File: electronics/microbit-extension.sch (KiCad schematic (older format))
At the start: 25 parts, among them SW1 SW_DIP_x01, SW2 SW_DIP_x01, SW3 SW_DIP_x01, SW4 SW_DIP_x01

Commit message: moved footprints to separate folder
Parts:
- removed U?: TLC5917ID, SOIC127P600X175-16N, symbol TLC5917ID
- added BZ?: Buzzer, symbol Buzzer
- added C? (x2): C, symbol C
- added D?: D, symbol D
- added R? (x2): 1K, symbol R
- added T?: 2N4401, TO92-CBE, symbol 2N4401
- added U?: LD1117S33CTR, TO_SOT_Packages_SMD:SOT-223, symbol LD1117S33CTR
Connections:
- net labels added: +9V, AI1, BUZZER_PIN
- wire segments 53 -> 87

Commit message: footprint assignment
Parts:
- removed D?: D, symbol D
- removed R?: 1K, symbol R
- C1: renamed from C?; value C -> 100nF
- C2: renamed from C?; value C -> 10uF
- gave numbers to parts that had none: 24
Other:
- moved on the sheet: BZ1, R9, T1

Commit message: removed temp files
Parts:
- BZ1: footprint (none) -> Buzzers_Beepers:BUZZER
- C1, C2: footprint (none) -> Capacitors_SMD:C_1210
- D1, D2, D3, D4, D5: footprint (none) -> LEDs:LED_D3.0mm
- D6: footprint (none) -> LEDs:LED_RGB_5050-6
- J1: footprint (none) -> Connectors_4UCON:4UCON_17909_02x401.27mm_Vertical
- R1, R10, R11, R12, R13, R2, R3, R4, R5, R6, R7, R8, R9: footprint (none) -> Resistors_SMD:R_1210
- RV1: footprint (none) -> Potentiometers:Potentiometer_Alps_RK09K_Horizontal
- SW1, SW2, SW3, SW4: footprint (none) -> Buttons_Switches_SMD:SW_SPST_B3S-1100
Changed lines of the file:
@@
 F 0 "J1" H 1350 4700 50  0000 C CNN
 F 1 "microbit_edge_connector" H 1350 4600 50  0000 C CNN
-F 2 "" H 1200 2550 50  0001 C CNN
+F 2 "Connectors_4UCON:4UCON_17909_02x401.27mm_Vertical" H 1200 2550 50  0001 C CNN
 F 3 "" H 1200 2550 50  0001 C CNN
 	1    1300 2650
@@
 F 0 "SW1" H 10600 1600 50  0000 C CNN
 F 1 "SW_DIP_x01" H 10600 1300 50  0000 C CNN
-F 2 "" H 10600 1450 50  0001 C CNN
+F 2 "Buttons_Switches_SMD:SW_SPST_B3S-1100" H 10600 1450 50  0001 C CNN
 F 3 "" H 10600 1450 50  0001 C CNN
 	1    10600 1450
@@
 F 0 "R10" V 10230 1250 50  0000 C CNN
 F 1 "R" V 10150 1250 50  0000 C CNN
-F 2 "" V 10080 1250 50  0001 C CNN
+F 2 "Resistors_SMD:R_1210" V 10080 1250 50  0001 C CNN
 F 3 "" H 10150 1250 50  0001 C CNN
 	1    10150 1250
@@
 F 0 "SW2" H 10600 2150 50  0000 C CNN
 F 1 "SW_DIP_x01" H 10600 1850 50  0000 C CNN
-F 2 "" H 10600 2000 50  0001 C CNN
+F 2 "Buttons_Switches_SMD:SW_SPST_B3S-1100" H 10600 2000 50  0001 C CNN
 F 3 "" H 10600 2000 50  0001 C CNN
 	1    10600 2000
@@
 F 0 "R11" V 10230 1800 50  0000 C CNN
 F 1 "R" V 10150 1800 50  0000 C CNN
-F 2 "" V 10080 1800 50  0001 C CNN
+F 2 "Resistors_SMD:R_1210" V 10080 1800 50  0001 C CNN
 F 3 "" H 10150 1800 50  0001 C CNN
 	1    10150 1800
@@
 F 0 "SW3" H 10600 2700 50  0000 C CNN
 F 1 "SW_DIP_x01" H 10600 2400 50  0000 C CNN
-F 2 "" H 10600 2550 50  0001 C CNN
+F 2 "Buttons_Switches_SMD:SW_SPST_B3S-1100" H 10600 2550 50  0001 C CNN
 F 3 "" H 10600 2550 50  0001 C CNN
 	1    10600 2550
@@
 F 0 "R12" V 10230 2350 50  0000 C CNN
 F 1 "R" V 10150 2350 50  0000 C CNN
-F 2 "" V 10080 2350 50  0001 C CNN
+F 2 "Resistors_SMD:R_1210" V 10080 2350 50  0001 C CNN
 F 3 "" H 10150 2350 50  0001 C CNN
 	1    10150 2350
@@
 F 0 "SW4" H 10600 3150 50  0000 C CNN
 F 1 "SW_DIP_x01" H 10600 2850 50  0000 C CNN
-F 2 "" H 10600 3000 50  0001 C CNN
+F 2 "Buttons_Switches_SMD:SW_SPST_B3S-1100" H 10600 3000 50  0001 C CNN
 F 3 "" H 10600 3000 50  0001 C CNN
 	1    10600 3000
@@
 F 0 "R13" V 10230 2800 50  0000 C CNN
 F 1 "R" V 10150 2800 50  0000 C CNN
-F 2 "" V 10080 2800 50  0001 C CNN
+F 2 "Resistors_SMD:R_1210" V 10080 2800 50  0001 C CNN
 F 3 "" H 10150 2800 50  0001 C CNN
 	1    10150 2800
@@
 F 0 "RV1" V 10425 4150 50  0000 C CNN
 F 1 "POT" V 10500 4150 50  0000 C CNN
-F 2 "" H 10600 4150 50  0001 C CNN
+F 2 "Potentiometers:Potentiometer_Alps_RK09K_Horizontal" H 10600 4150 50  0001 C CNN
 F 3 "" H 10600 4150 50  0001 C CNN
 	1    10600 4150
@@
 F 0 "D1" H 8800 1250 50  0000 C CNN
 F 1 "LED" H 8800 1050 50  0000 C CNN
-F 2 "" H 8800 1150 50  0001 C CNN
+F 2 "LEDs:LED_D3.0mm" H 8800 1150 50  0001 C CNN
 F 3 "" H 8800 1150 50  0001 C CNN
 	1    8800 1150
@@
 F 0 "R1" V 8430 1150 50  0000 C CNN
 F 1 "R" V 8350 1150 50  0000 C CNN
-F 2 "" V 8280 1150 50  0001 C CNN
+F 2 "Resistors_SMD:R_1210" V 8280 1150 50  0001 C CNN
 F 3 "" H 8350 1150 50  0001 C CNN
 	1    8350 1150
@@
 F 0 "D3" H 8800 1850 50  0000 C CNN
 F 1 "LED" H 8800 1650 50  0000 C CNN
-F 2 "" H 8800 1750 50  0001 C CNN
+F 2 "LEDs:LED_D3.0mm" H 8800 1750 50  0001 C CNN
 F 3 "" H 8800 1750 50  0001 C CNN
 	1    8800 1750
@@
 F 0 "R3" V 8430 1750 50  0000 C CNN
 F 1 "R" V 8350 1750 50  0000 C CNN
-F 2 "" V 8280 1750 50  0001 C CNN
+F 2 "Resistors_SMD:R_1210" V 8280 1750 50  0001 C CNN
 F 3 "" H 8350 1750 50  0001 C CNN
 	1    8350 1750
@@
 F 0 "D2" H 8800 1550 50  0000 C CNN
 F 1 "LED" H 8800 1350 50  0000 C CNN
-F 2 "" H 8800 1450 50  0001 C CNN
+F 2 "LEDs:LED_D3.0mm" H 8800 1450 50  0001 C CNN
 F 3 "" H 8800 1450 50  0001 C CNN
 	1    8800 1450
@@
 F 0 "R2" V 8430 1450 50  0000 C CNN
 F 1 "R" V 8350 1450 50  0000 C CNN
-F 2 "" V 8280 1450 50  0001 C CNN
+F 2 "Resistors_SMD:R_1210" V 8280 1450 50  0001 C CNN
 F 3 "" H 8350 1450 50  0001 C CNN
 	1    8350 1450
@@
 F 0 "D4" H 8800 2150 50  0000 C CNN
 F 1 "LED" H 8800 1950 50  0000 C CNN
-F 2 "" H 8800 2050 50  0001 C CNN
+F 2 "LEDs:LED_D3.0mm" H 8800 2050 50  0001 C CNN
 F 3 "" H 8800 2050 50  0001 C CNN
 	1    8800 2050
@@
 F 0 "R4" V 8430 2050 50  0000 C CNN
 F 1 "R" V 8350 2050 50  0000 C CNN
-F 2 "" V 8280 2050 50  0001 C CNN
+F 2 "Resistors_SMD:R_1210" V 8280 2050 50  0001 C CNN
 F 3 "" H 8350 2050 50  0001 C CNN
 	1    8350 2050
@@
 F 0 "D5" H 8800 2450 50  0000 C CNN
 F 1 "LED" H 8800 2250 50  0000 C CNN
-F 2 "" H 8800 2350 50  0001 C CNN
+F 2 "LEDs:LED_D3.0mm" H 8800 2350 50  0001 C CNN
 F 3 "" H 8800 2350 50  0001 C CNN
 	1    8800 2350
@@
 F 0 "R5" V 8430 2350 50  0000 C CNN
 F 1 "R" V 8350 2350 50  0000 C CNN
-F 2 "" V 8280 2350 50  0001 C CNN
+F 2 "Resistors_SMD:R_1210" V 8280 2350 50  0001 C CNN
 F 3 "" H 8350 2350 50  0001 C CNN
 	1    8350 2350
@@
 F 0 "D6" H 8800 3320 50  0000 C CNN
 F 1 "LED_RGB" H 8800 2600 50  0000 C CNN
-F 2 "" H 8800 2900 50  0001 C CNN
+F 2 "LEDs:LED_RGB_5050-6" H 8800 2900 50  0001 C CNN
 F 3 "" H 8800 2900 50  0001 C CNN
 	1    8800 2950
@@
 F 0 "R6" V 8250 2750 50  0000 C CNN
 F 1 "R" V 8350 2750 50  0000 C CNN
-F 2 "" V 8280 2750 50  0001 C CNN
+F 2 "Resistors_SMD:R_1210" V 8280 2750 50  0001 C CNN
 F 3 "" H 8350 2750 50  0001 C CNN
 	1    8350 2750
@@
 F 0 "R7" V 8250 2950 50  0000 C CNN
 F 1 "R" V 8350 2950 50  0000 C CNN
-F 2 "" V 8280 2950 50  0001 C CNN
+F 2 "Resistors_SMD:R_1210" V 8280 2950 50  0001 C CNN
 F 3 "" H 8350 2950 50  0001 C CNN
 	1    8350 2950
@@
 F 0 "R8" V 8250 3150 50  0000 C CNN
 F 1 "R" V 8350 3150 50  0000 C CNN
-F 2 "" V 8280 3150 50  0001 C CNN
+F 2 "Resistors_SMD:R_1210" V 8280 3150 50  0001 C CNN
 F 3 "" H 8350 3150 50  0001 C CNN
 	1    8350 3150
@@
 F 0 "BZ1" H 10850 5300 50  0000 L CNN
 F 1 "Buzzer" H 10850 5200 50  0000 L CNN
-F 2 "" V 10675 5350 50  0001 C CNN
+F 2 "Buzzers_Beepers:BUZZER" V 10675 5350 50  0001 C CNN
 F 3 "" V 10675 5350 50  0001 C CNN
 	1    10700 5250
@@
 F 0 "R9" V 10280 5650 50  0000 C CNN
 F 1 "1K" V 10200 5650 50  0000 C CNN
-F 2 "" V 10130 5650 50  0001 C CNN
+F 2 "Resistors_SMD:R_1210" V 10130 5650 50  0001 C CNN
 F 3 "" H 10200 5650 50  0001 C CNN
 	1    10200 5650
@@
 F 0 "C1" H 8175 4500 50  0000 L CNN
 F 1 "100nF" H 8175 4300 50  0000 L CNN
-F 2 "" H 8188 4250 50  0001 C CNN
+F 2 "Capacitors_SMD:C_1210" H 8188 4250 50  0001 C CNN
 F 3 "" H 8150 4400 50  0001 C CNN
 	1    8150 4400
@@
 F 0 "C2" H 9225 4500 50  0000 L CNN
 F 1 "10uF" H 9225 4300 50  0000 L CNN
-F 2 "" H 9238 4250 50  0001 C CNN
+F 2 "Capacitors_SMD:C_1210" H 9238 4250 50  0001 C CNN
 F 3 "" H 9200 4400 50  0001 C CNN
 	1    9200 4400

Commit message: more updates to schematic
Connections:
- net +3V3: now also J1.17 (P18_3v3), J1.27 (P17_3v3)
- net AI1: now also J1.55 (P1), J1.57 (P1), J1.59 (P1), J1.61 (P1); no longer RV1.2
- net GND: now also J1.11 (P21_GND)
- net LED0: now also J1.29 (P16)
- net LED1: now also J1.45 (P12)
- net LED2: now also J1.49 (P10)
- net LED3: now also J1.51 (P9)
- net LED4: now also J1.53 (P8)
- net SDA: now reaches J1.13 (P20_SDA)
- net SCL: now reaches J1.15 (P19_SCL)
- net MOSI: now reaches J1.31 (P15_MOSI)
- net MISO: now reaches J1.33 (P14_MISO)
- net SCK: now reaches J1.35 (P13_SCK)
- net AI2: now reaches J1.37 (P2)
- net AI2: now also J1.39 (P2), J1.41 (P2), J1.43 (P2)
- net BUT_B: now reaches J1.47 (P11_Button_B)
- net BUT_A: now reaches J1.67 (P5_Button_A)
- net AI0: now reaches J1.71 (P0)
- net AI0: now also J1.73 (P0), J1.75 (P0), J1.77 (P0), RV1.2
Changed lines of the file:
@@
 $EndComp
 Wire Wire Line
-	1800 850  1800 1250
+	1800 850  1800 1350
 Connection ~ 1800 1150
 Connection ~ 1800 1050
@@
 Connection ~ 9050 2350
 Wire Wire Line
-	1800 1750 1800 2050
+	1800 1650 1800 2150
 Connection ~ 1800 1850
 Connection ~ 1800 1950
@@
 	10450 4150 9950 4150
 Text Label 9950 4150 0    60   ~ 0
-AI1
+AI0
 $Comp
 L Buzzer BZ1
@@
 Wire Wire Line
 	10600 5000 10600 5150
+Wire Wire Line
+	1800 2650 1800 2950
+Connection ~ 1800 2750
+Connection ~ 1800 2850
+Wire Wire Line
+	1800 3550 1800 3850
+Connection ~ 1800 3750
+Connection ~ 1800 3650
+Wire Wire Line
+	1800 3700 2100 3700
+Connection ~ 1800 3700
+Text Label 2100 3700 2    60   ~ 0
+AI1
+Wire Wire Line
+	1800 4350 1800 4650
+Connection ~ 1800 4450
+Connection ~ 1800 4550
+Text Label 2100 4500 2    60   ~ 0
+AI0
+Wire Wire Line
+	1800 4500 2100 4500
+Connection ~ 1800 4500
+Wire Wire Line
+	1800 2800 2100 2800
+Connection ~ 1800 2800
+Text Label 2100 2800 2    60   ~ 0
+AI2
+Connection ~ 1800 1750
+Connection ~ 1800 1250
+Wire Wire Line
+	1800 1450 2050 1450
+Wire Wire Line
+	1800 1550 2050 1550
+Text Label 2050 1450 2    60   ~ 0
+SDA
+Text Label 2050 1550 2    60   ~ 0
+SCL
+Wire Wire Line
+	1800 2350 2100 2350
+Wire Wire Line
+	1800 2450 2100 2450
+Wire Wire Line
+	1800 2550 2100 2550
+Text Label 2100 2350 2    60   ~ 0
+MOSI
+Text Label 2100 2450 2    60   ~ 0
+MISO
+Text Label 2100 2550 2    60   ~ 0
+SCK
+Connection ~ 1800 2050
+Wire Wire Line
+	1800 2250 2100 2250
+Text Label 2100 2250 2    60   ~ 0
+LED0
+Wire Wire Line
+	1800 3150 2100 3150
+Text Label 2100 3150 2    60   ~ 0
+BUT_B
+Wire Wire Line
+	1800 4150 2100 4150
+Text Label 2100 4150 2    60   ~ 0
+BUT_A
+Wire Wire Line
+	1800 3050 2100 3050
+Text Label 2100 3050 2    60   ~ 0
+LED1
+Wire Wire Line
+	1800 3250 2100 3250
+Text Label 2100 3250 2    60   ~ 0
+LED2
+Text Label 2100 3350 2    60   ~ 0
+LED3
+Wire Wire Line
+	1800 3350 2100 3350
+Wire Wire Line
+	1800 3450 2100 3450
+Text Label 2100 3450 2    60   ~ 0
+LED4
 $EndSCHEMATC

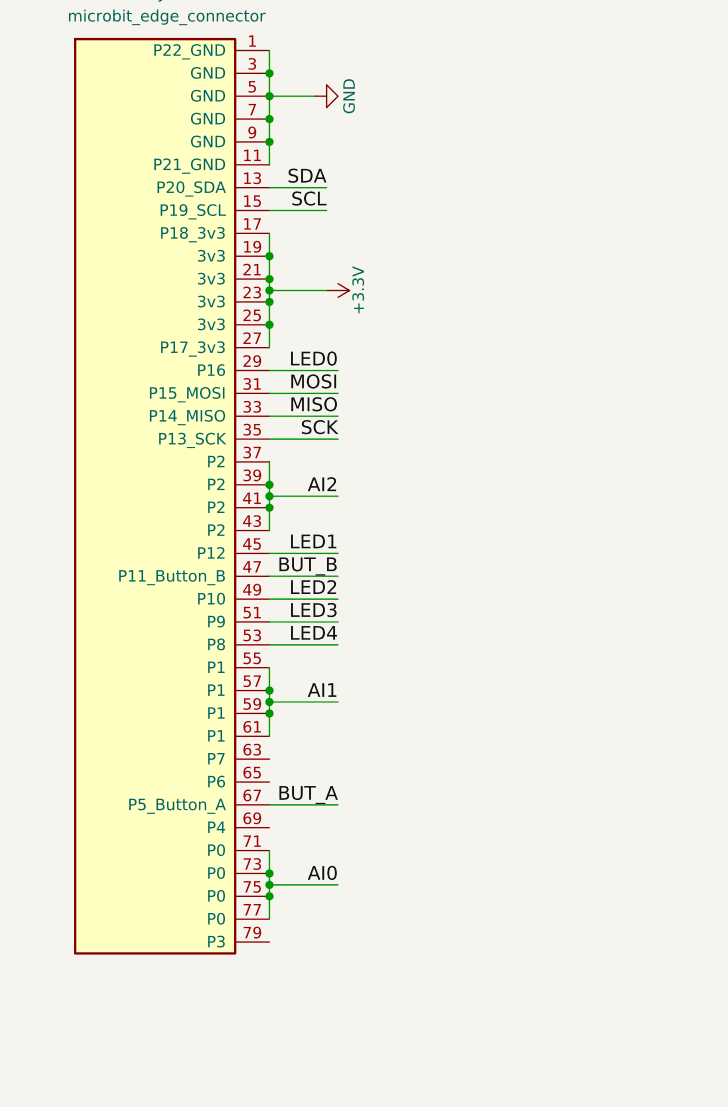
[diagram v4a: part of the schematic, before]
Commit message: added final local connections, need to check through
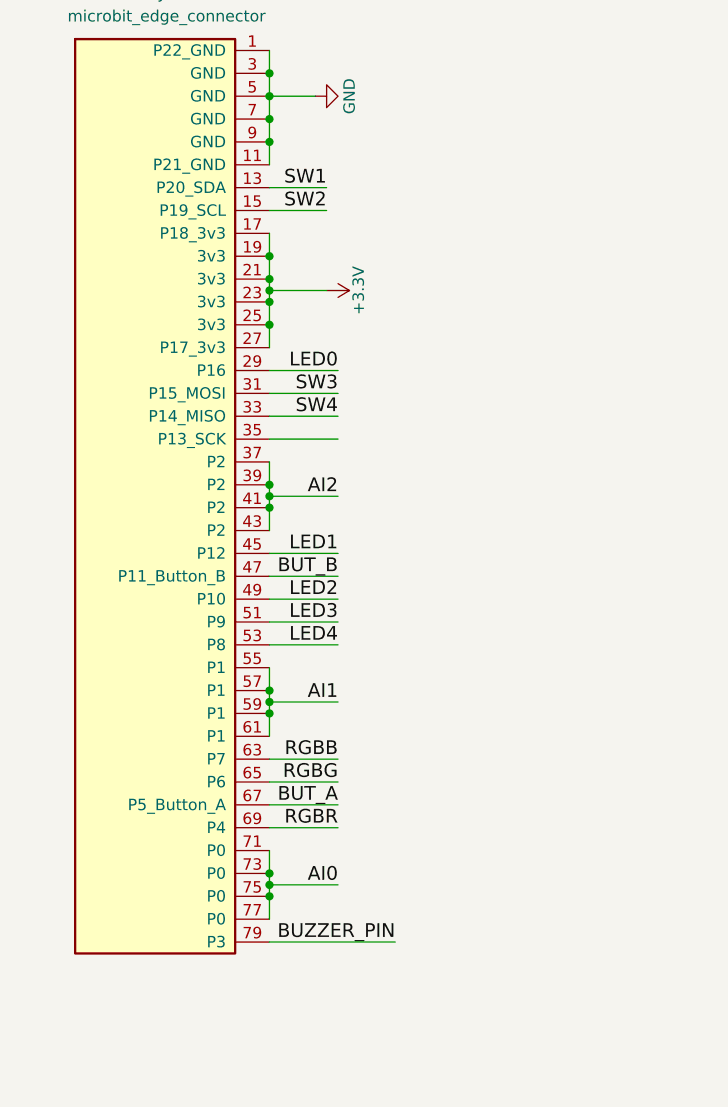
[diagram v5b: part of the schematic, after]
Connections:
- net MISO is gone; now on net SW4: J1.33 (P14_MISO)
- net MOSI is gone; now on net SW3: J1.31 (P15_MOSI)
- net SCL is gone; now on net SW2: J1.15 (P19_SCL)
- net SDA is gone; now on net SW1: J1.13 (P20_SDA)
- net BUZZER_PIN: now also J1.79 (P3)
- net RGBB: now also J1.63 (P7)
- net RGBG: now also J1.65 (P6)
- net RGBR: now also J1.69 (P4)
- net SCK: no longer names the net of J1.35 (P13_SCK)
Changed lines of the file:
@@
 Wire Wire Line
 	1800 1550 2050 1550
-Text Label 2050 1450 2    60   ~ 0
-SDA
-Text Label 2050 1550 2    60   ~ 0
-SCL
 Wire Wire Line
 	1800 2350 2100 2350
@@
 Wire Wire Line
 	1800 2550 2100 2550
-Text Label 2100 2350 2    60   ~ 0
-MOSI
-Text Label 2100 2450 2    60   ~ 0
-MISO
-Text Label 2100 2550 2    60   ~ 0
-SCK
 Connection ~ 1800 2050
 Wire Wire Line
@@
 Text Label 2100 3450 2    60   ~ 0
 LED4
+Text Label 2100 3950 2    60   ~ 0
+RGBB
+Wire Wire Line
+	1800 3950 2100 3950
+Wire Wire Line
+	1800 4050 2100 4050
+Text Label 2100 4050 2    60   ~ 0
+RGBG
+Wire Wire Line
+	1800 4250 2100 4250
+Text Label 2100 4250 2    60   ~ 0
+RGBR
+Wire Wire Line
+	1800 4750 2350 4750
+Text Label 2050 1450 2    60   ~ 0
+SW1
+Text Label 2050 1550 2    60   ~ 0
+SW2
+Text Label 2100 2350 2    60   ~ 0
+SW3
+Text Label 2100 2450 2    60   ~ 0
+SW4
+Text Label 2350 4750 2    60   ~ 0
+BUZZER_PIN
 $EndSCHEMATC

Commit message: update to schematics
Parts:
- C1, C2: footprint Capacitors_SMD:C_1210 -> Capacitors_SMD:C_0805
- R1, R10, R11, R12, R13, R2, R3, R4, R5, R6, R7, R8, R9: footprint Resistors_SMD:R_1210 -> Resistors_SMD:R_0805
- SW1, SW2, SW3, SW4: footprint Buttons_Switches_SMD:SW_SPST_B3S-1100 -> Buttons_Switches_SMD:SW_SPST_EVPBF
- T1: footprint TO92-CBE -> (none)
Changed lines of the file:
@@
 F 0 "SW1" H 10600 1600 50  0000 C CNN
 F 1 "SW_DIP_x01" H 10600 1300 50  0000 C CNN
-F 2 "Buttons_Switches_SMD:SW_SPST_B3S-1100" H 10600 1450 50  0001 C CNN
+F 2 "Buttons_Switches_SMD:SW_SPST_EVPBF" H 10600 1450 50  0001 C CNN
 F 3 "" H 10600 1450 50  0001 C CNN
 	1    10600 1450
@@
 F 0 "R10" V 10230 1250 50  0000 C CNN
 F 1 "R" V 10150 1250 50  0000 C CNN
-F 2 "Resistors_SMD:R_1210" V 10080 1250 50  0001 C CNN
+F 2 "Resistors_SMD:R_0805" V 10080 1250 50  0001 C CNN
 F 3 "" H 10150 1250 50  0001 C CNN
 	1    10150 1250
@@
 F 0 "SW2" H 10600 2150 50  0000 C CNN
 F 1 "SW_DIP_x01" H 10600 1850 50  0000 C CNN
-F 2 "Buttons_Switches_SMD:SW_SPST_B3S-1100" H 10600 2000 50  0001 C CNN
+F 2 "Buttons_Switches_SMD:SW_SPST_EVPBF" H 10600 2000 50  0001 C CNN
 F 3 "" H 10600 2000 50  0001 C CNN
 	1    10600 2000
@@
 F 0 "R11" V 10230 1800 50  0000 C CNN
 F 1 "R" V 10150 1800 50  0000 C CNN
-F 2 "Resistors_SMD:R_1210" V 10080 1800 50  0001 C CNN
+F 2 "Resistors_SMD:R_0805" V 10080 1800 50  0001 C CNN
 F 3 "" H 10150 1800 50  0001 C CNN
 	1    10150 1800
@@
 F 0 "SW3" H 10600 2700 50  0000 C CNN
 F 1 "SW_DIP_x01" H 10600 2400 50  0000 C CNN
-F 2 "Buttons_Switches_SMD:SW_SPST_B3S-1100" H 10600 2550 50  0001 C CNN
+F 2 "Buttons_Switches_SMD:SW_SPST_EVPBF" H 10600 2550 50  0001 C CNN
 F 3 "" H 10600 2550 50  0001 C CNN
 	1    10600 2550
@@
 F 0 "R12" V 10230 2350 50  0000 C CNN
 F 1 "R" V 10150 2350 50  0000 C CNN
-F 2 "Resistors_SMD:R_1210" V 10080 2350 50  0001 C CNN
+F 2 "Resistors_SMD:R_0805" V 10080 2350 50  0001 C CNN
 F 3 "" H 10150 2350 50  0001 C CNN
 	1    10150 2350
@@
 F 0 "SW4" H 10600 3150 50  0000 C CNN
 F 1 "SW_DIP_x01" H 10600 2850 50  0000 C CNN
-F 2 "Buttons_Switches_SMD:SW_SPST_B3S-1100" H 10600 3000 50  0001 C CNN
+F 2 "Buttons_Switches_SMD:SW_SPST_EVPBF" H 10600 3000 50  0001 C CNN
 F 3 "" H 10600 3000 50  0001 C CNN
 	1    10600 3000
@@
 F 0 "R13" V 10230 2800 50  0000 C CNN
 F 1 "R" V 10150 2800 50  0000 C CNN
-F 2 "Resistors_SMD:R_1210" V 10080 2800 50  0001 C CNN
+F 2 "Resistors_SMD:R_0805" V 10080 2800 50  0001 C CNN
 F 3 "" H 10150 2800 50  0001 C CNN
 	1    10150 2800
@@
 F 0 "R1" V 8430 1150 50  0000 C CNN
 F 1 "R" V 8350 1150 50  0000 C CNN
-F 2 "Resistors_SMD:R_1210" V 8280 1150 50  0001 C CNN
+F 2 "Resistors_SMD:R_0805" V 8280 1150 50  0001 C CNN
 F 3 "" H 8350 1150 50  0001 C CNN
 	1    8350 1150
@@
 F 0 "R3" V 8430 1750 50  0000 C CNN
 F 1 "R" V 8350 1750 50  0000 C CNN
-F 2 "Resistors_SMD:R_1210" V 8280 1750 50  0001 C CNN
+F 2 "Resistors_SMD:R_0805" V 8280 1750 50  0001 C CNN
 F 3 "" H 8350 1750 50  0001 C CNN
 	1    8350 1750
@@
 F 0 "R2" V 8430 1450 50  0000 C CNN
 F 1 "R" V 8350 1450 50  0000 C CNN
-F 2 "Resistors_SMD:R_1210" V 8280 1450 50  0001 C CNN
+F 2 "Resistors_SMD:R_0805" V 8280 1450 50  0001 C CNN
 F 3 "" H 8350 1450 50  0001 C CNN
 	1    8350 1450
@@
 F 0 "R4" V 8430 2050 50  0000 C CNN
 F 1 "R" V 8350 2050 50  0000 C CNN
-F 2 "Resistors_SMD:R_1210" V 8280 2050 50  0001 C CNN
+F 2 "Resistors_SMD:R_0805" V 8280 2050 50  0001 C CNN
 F 3 "" H 8350 2050 50  0001 C CNN
 	1    8350 2050
@@
 F 0 "R5" V 8430 2350 50  0000 C CNN
 F 1 "R" V 8350 2350 50  0000 C CNN
-F 2 "Resistors_SMD:R_1210" V 8280 2350 50  0001 C CNN
+F 2 "Resistors_SMD:R_0805" V 8280 2350 50  0001 C CNN
 F 3 "" H 8350 2350 50  0001 C CNN
 	1    8350 2350
@@
 F 0 "R6" V 8250 2750 50  0000 C CNN
 F 1 "R" V 8350 2750 50  0000 C CNN
-F 2 "Resistors_SMD:R_1210" V 8280 2750 50  0001 C CNN
+F 2 "Resistors_SMD:R_0805" V 8280 2750 50  0001 C CNN
 F 3 "" H 8350 2750 50  0001 C CNN
 	1    8350 2750
@@
 F 0 "R7" V 8250 2950 50  0000 C CNN
 F 1 "R" V 8350 2950 50  0000 C CNN
-F 2 "Resistors_SMD:R_1210" V 8280 2950 50  0001 C CNN
+F 2 "Resistors_SMD:R_0805" V 8280 2950 50  0001 C CNN
 F 3 "" H 8350 2950 50  0001 C CNN
 	1    8350 2950
@@
 F 0 "R8" V 8250 3150 50  0000 C CNN
 F 1 "R" V 8350 3150 50  0000 C CNN
-F 2 "Resistors_SMD:R_1210" V 8280 3150 50  0001 C CNN
+F 2 "Resistors_SMD:R_0805" V 8280 3150 50  0001 C CNN
 F 3 "" H 8350 3150 50  0001 C CNN
 	1    8350 3150
@@
 F 0 "T1" H 10099 5950 50  0000 L BNN
 F 1 "2N4401" H 10100 5850 50  0000 L BNN
-F 2 "TO92-CBE" H 10500 5650 50  0001 L BNN
+F 2 "" H 10500 5650 50  0001 L BNN
 F 3 "Multicomp" H 10500 5650 50  0001 L BNN
 F 4 "BIPOLAR TRANSISTOR%2C NPN%2C TO-92%3B Transistor Polarity%3A NPN%3B Collector Emitter Voltage V%28br%29ceo%3A 40V%3B Transition Frequen..." H 10500 5650 50  0001 L BNN "Description"
@@
 F 0 "R9" V 10280 5650 50  0000 C CNN
 F 1 "1K" V 10200 5650 50  0000 C CNN
-F 2 "Resistors_SMD:R_1210" V 10130 5650 50  0001 C CNN
+F 2 "Resistors_SMD:R_0805" V 10130 5650 50  0001 C CNN
 F 3 "" H 10200 5650 50  0001 C CNN
 	1    10200 5650
@@
 F 0 "C1" H 8175 4500 50  0000 L CNN
 F 1 "100nF" H 8175 4300 50  0000 L CNN
-F 2 "Capacitors_SMD:C_1210" H 8188 4250 50  0001 C CNN
+F 2 "Capacitors_SMD:C_0805" H 8188 4250 50  0001 C CNN
 F 3 "" H 8150 4400 50  0001 C CNN
 	1    8150 4400
@@
 F 0 "C2" H 9225 4500 50  0000 L CNN
 F 1 "10uF" H 9225 4300 50  0000 L CNN
-F 2 "Capacitors_SMD:C_1210" H 9238 4250 50  0001 C CNN
+F 2 "Capacitors_SMD:C_0805" H 9238 4250 50  0001 C CNN
 F 3 "" H 9200 4400 50  0001 C CNN
 	1    9200 4400

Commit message: finishing up routing
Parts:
- added J2: 9V conn, Pin_Headers:Pin_Header_Straight_1x02_Pitch2.54mm, symbol CONN_01X02
- T1: footprint (none) -> TO_SOT_Packages_SMD:SOT-23
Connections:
- net +9V: now also J2.1 (P1)
- net GND: now also J2.2 (P2)
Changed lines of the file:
@@
 F 0 "T1" H 10099 5950 50  0000 L BNN
 F 1 "2N4401" H 10100 5850 50  0000 L BNN
-F 2 "" H 10500 5650 50  0001 L BNN
+F 2 "TO_SOT_Packages_SMD:SOT-23" H 10500 5650 50  0001 L BNN
 F 3 "Multicomp" H 10500 5650 50  0001 L BNN
 F 4 "BIPOLAR TRANSISTOR%2C NPN%2C TO-92%3B Transistor Polarity%3A NPN%3B Collector Emitter Voltage V%28br%29ceo%3A 40V%3B Transition Frequen..." H 10500 5650 50  0001 L BNN "Description"
@@
 	0    1    1    0
 $EndComp
-Wire Wire Line
-	10350 5650 10400 5650
 $Comp
 L GND #PWR012
@@
 	0    1    1    0
 $EndComp
-Wire Wire Line
-	10600 5350 10600 5450
 Wire Wire Line
 	10600 5000 10600 5150
@@
 Text Label 2350 4750 2    60   ~ 0
 BUZZER_PIN
+$Comp
+L CONN_01X02 J2
+U 1 1 598C7F0A
+P 8650 5300
+F 0 "J2" H 8650 5450 50  0000 C CNN
+F 1 "9V conn" V 8750 5300 50  0000 C CNN
+F 2 "Pin_Headers:Pin_Header_Straight_1x02_Pitch2.54mm" H 8650 5300 50  0001 C CNN
+F 3 "" H 8650 5300 50  0001 C CNN
+	1    8650 5300
+	1    0    0    -1
+$EndComp
+$Comp
+L +9V #PWR016
+U 1 1 598C8024
+P 8450 5250
+F 0 "#PWR016" H 8450 5100 50  0001 C CNN
+F 1 "+9V" H 8450 5390 50  0000 C CNN
+F 2 "" H 8450 5250 50  0001 C CNN
+F 3 "" H 8450 5250 50  0001 C CNN
+	1    8450 5250
+	0    -1   -1   0
+$EndComp
+$Comp
+L GND #PWR017
+U 1 1 598C808C
+P 8450 5350
+F 0 "#PWR017" H 8450 5100 50  0001 C CNN
+F 1 "GND" H 8450 5200 50  0000 C CNN
+F 2 "" H 8450 5350 50  0001 C CNN
+F 3 "" H 8450 5350 50  0001 C CNN
+	1    8450 5350
+	0    1    1    0
+$EndComp
+Wire Wire Line
+	10600 5350 10600 5450
+Wire Wire Line
+	10350 5650 10400 5650
 $EndSCHEMATC
